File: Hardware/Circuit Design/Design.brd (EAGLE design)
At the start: 94 x 38.1 mm, 41 parts, among them J1 6495, U1 ATMEGA328-PU, U2 TP4056, U3 HTU21D, U4 MT3608, Y1 16 MHz HC-49US

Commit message: Design display for co2 monitor
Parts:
- added U$2: LOGO, PCB Logo:FOOTPRINT
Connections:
- net +5V: now also FTDI_PROG.TX, U$1.VIN; no longer FTDI_PROG.VCC, U$1.PWM
- net GND: now also U$1.GND; no longer U$1.AOT
- net MHZ-TX: now also U$1.RX; no longer U$1.SR
- net RX: now also FTDI_PROG.VCC; no longer FTDI_PROG.TX
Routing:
- net MHZ-TX: track 58.0 -> 62.5 mm

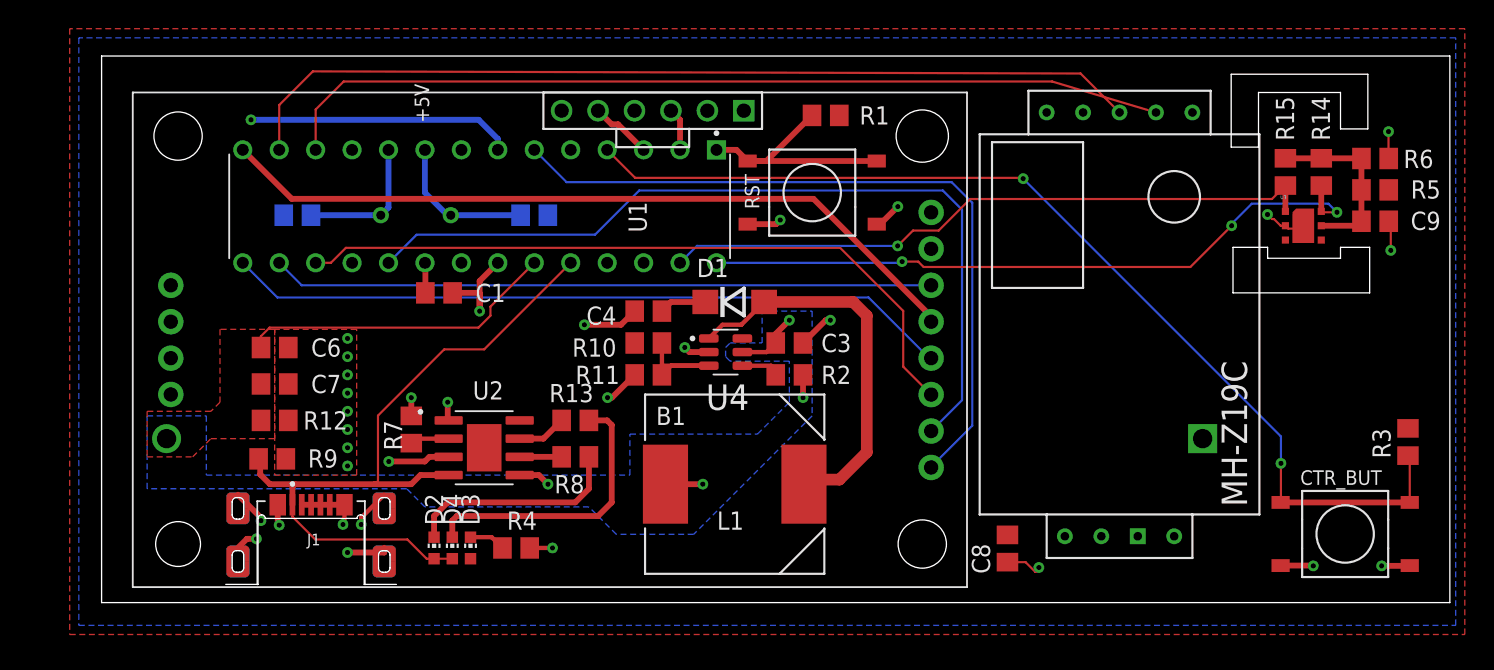
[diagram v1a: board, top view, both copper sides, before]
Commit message: Correct the sleep mode enter function and add the new board design
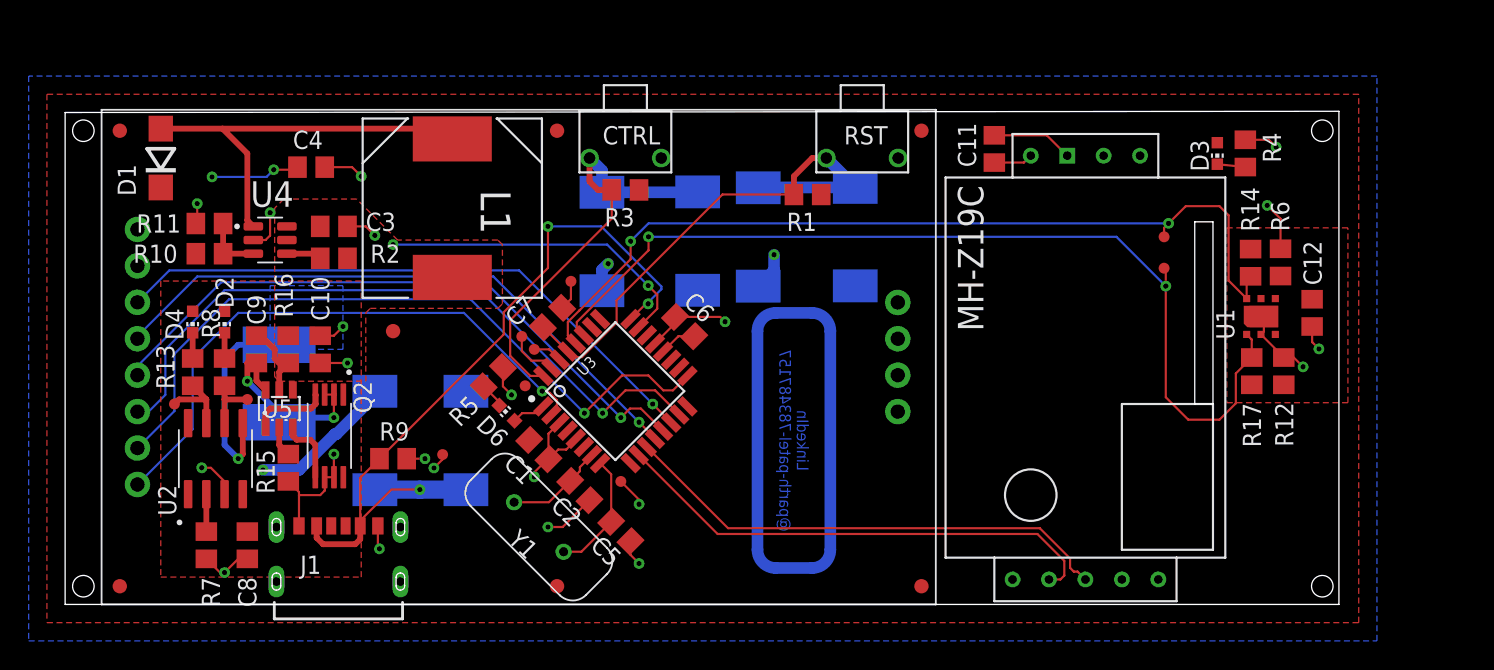
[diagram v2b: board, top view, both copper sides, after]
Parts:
- removed B1: 1S, 18650 1S PCB Mount:18650-1S-DIP
- removed FTDI_PROG: UART, FTDI Adapter:UART
- added BAT+, BAT-: WIREPADSMD5-2,5, wirepad:5-2,5
- added C10: 10u, rcl:C0805
- added C11: 47u, rcl:C0805
- added C12: 100n, rcl:C0805
- added D10, D11, D12, D7, D8, D9: SS310, Schottky SS310:DIOM6859X262N
- added D6: 5215, led:CHIP-LED0603
- added FID1, FID2, FID3, FID4, FID5, FID6, FID7: FIDUCIAL"", Airquality_Sensor:FIDUCIAL_1MM
- added Q2: FS8205A, FS8205A:SOP65P640X120-8N
- added R16: 100R, rcl:R0805
- added R17: 10k, rcl:R0805
- added TP1, TP10, TP2, TP3, TP4, TP5, TP6, TP7: TEST-POINT3, SparkFun-Connectors:PAD.03X.03
- added TP8: ~STDBY, SparkFun-Connectors:PAD.03X.03
- added TP9: ~CHRG, SparkFun-Connectors:PAD.03X.03
- added U5: DW01A, DW01A:SOT23-6
- C6: value 10u -> 100n
- C7: value 100n -> 10u
- C8: value 47u -> 10u
- CTR_BUT, RST: value 4.5X4.5-SMD-TACTILE-SWITCH -> 7058; device Switches:SMD-4.5X4.5-TACTILE-PUSH-BUTTON -> Switches:DIP_3X6MM_SIDE_PRESS_2PIN
- D2: value BLUE -> 5216
- D3: value RED -> 5215
- D4: value ORANGE -> 5215
- J1: value 6495 -> 5362; device MicroUSB Type B Socket:AMPHENOL_10103593-0001LF -> MicroUSB Type C Socket:GCT_USB4125-GF-A-0190_REVA2
- L1: value 220uH -> 22uH
- R12: value 10k -> 3k
- R15: value 10k -> 1k
- R5: value 1.8k -> 220R
- R6: value 3k -> 1.8k
- R7: value 1.2k -> 3k
- U$1: value MH-Z19C -> LOGO_17MM; device MH-Z19 Sensor:MH-Z19C -> PCB Logo:FOOTPRINT_17MM
- U$2: value LOGO -> MH-Z19C; device PCB Logo:FOOTPRINT -> MH-Z19 Sensor:MH-Z19C
- U1: value ATMEGA328-PU -> HTU21D; device ATMEGA328-PU:DIP787W46P254L3467H508Q28 -> HTU21D:QFN100P300X300X100-7N
- U3: value HTU21D -> ATMEGA328P-AU; device HTU21D:QFN100P300X300X100-7N -> ATMEGA328P-AU:QFP80P900X900X120-32N
- Y1: value 16 MHz HC-49US -> HC-49US
- moved C9 78.5 mm to (10.8, 17.8), turned to 270 degrees
- moved R15 72.5 mm to (13.0, 9.53), turned to 270 degrees
- moved R12 70.4 mm to (82.4, 16.3), turned to 270 degrees
- moved DISPLAY 70.1 mm to (0.00, 0.00), turned to 0 degrees
- moved R5 62.8 mm to (27.3, 15.9), turned to 45 degrees
- moved D3 58.9 mm to (77.8, 31.4), turned to 180 degrees
- moved R4 57.8 mm to (79.7, 31.4), turned to 90 degrees
- moved R3 57.3 mm to (36.5, 28.9), turned to 180 degrees
- moved CTR_BUT 56.6 mm to (36.5, 31.1), turned to 180 degrees
- moved U1 55.0 mm to (80.8, 20.1), turned to 90 degrees
- moved C8 53.0 mm to (10.2, 4.13)
- moved U3 49.3 mm to (35.8, 14.9), turned to 45 degrees
- moved D1 41.2 mm to (4.13, 31.1), turned to 90 degrees
- moved C3 32.8 mm to (16.2, 26.4)
- moved R2 32.8 mm to (16.2, 24.1)
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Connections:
- removed net MHZ-RX: U$1.TX, U1.13
- removed net MHZ-TX: U$1.RX, U1.12
- removed net MISO: U1.18
- removed net N$1: R8.2, U2.6
- removed net N$4: R7.2, U2.2
- new net BAT-: BAT-.1, C9.2, Q2.2, Q2.3, U5.6
- new net DTR: C7.2, TP1.P$1
- new net MHZ_N: U$2.RX, U3.10
- new net MHZ_P: U$2.TX, U3.11
- new net N$13: D6.C, R5.1
- new net N$14: D6.A, U3.1
- new net N$15: Q2.5, U5.3
- new net N$16: R13.2, TP9.P$1, U2.7
- new net N$17: R8.2, TP8.P$1, U2.6
- new net N$18: R7.1, U2.2
- new net N$19: Q2.4, U5.1
- new net N$20: R15.1, U5.2
- new net N$21: C9.1, R16.1, U5.5
- new net SUP-IN: D7.A, D8.C, J1.A9, J1.B9, R9.1, U3.24
- net +3V3: now also C12.1, R12.2, R17.2, R6.1, U1.5; no longer C9.1, R15.2, R5.1, R6.2, U3.5
- net +5V: now also C11.1, D11.C, D9.C, DISPLAY.VCC, R6.2, TP4.P$1, U$2.VIN, U3.18, U3.4, U3.6; no longer C8.1, DISPLAY.P$16, FTDI_PROG.TX, R5.2, U$1.VIN, U1.20, U1.7
- net CTR-BTN: now also CTR_BUT.P$1, D10.C, D9.A, U3.32; no longer CTR_BUT.1.1, CTR_BUT.1.2, U1.4
- net GND: now also C10.2, C11.2, C12.2, CTR_BUT.P$2, D10.A, D12.A, D8.A, DISPLAY.GND, J1.A12, J1.B12, Q2.6, Q2.7, R15.2, R5.2, R7.2, RST.P$2, TP5.P$1, TP7.P$1, U$2.GND, U1.2, U1.PAD, U3.21, U3.3, U3.5; no longer B1.V-, C7.2, C9.2, CTR_BUT.2.1, CTR_BUT.2.2, DISPLAY.P$15, FTDI_PROG.GND, J1.2, J1.3, J1.4, J1.5, J1.S1, J1.S2, J1.S3, J1.S4, J1.S5, J1.S6, R6.1, R7.1, RST.2.1, RST.2.2, U$1.GND, U1.22, U1.8, U2.1, U3.2, U3.PAD
- net MOSI: now also DISPLAY.SDA, U3.15; no longer DISPLAY.P$11, U1.17
- net N$10: now also U3.7; no longer U1.9
- net N$2: now also U3.8; no longer U1.10
- net N$6: now also C6.1, U3.20; no longer R13.2, U2.7
- net RST: now also C7.1, D11.A, D12.C, RST.P$1, U3.29; no longer RST.1.1, RST.1.2, U1.1
- net RX: now also TP2.P$1, U3.30; no longer FTDI_PROG.VCC, U1.2
- net SCK: now also DISPLAY.SCK, U3.17; no longer DISPLAY.P$10, U1.19
- net SCL: now also TP6.P$1, U1.6, U3.28; no longer U1.28, U3.6
- net SDA: now also R17.1, TP10.P$1, U1.1, U3.27; no longer R15.1, U1.27, U3.1
- net TFT-CS: now also DISPLAY.CS, U3.14; no longer DISPLAY.P$14, U1.16
- net TFT-DC: now also DISPLAY.DC, U3.13; no longer DISPLAY.P$12, U1.15
- net TFT-LED: now also DISPLAY.LED, U3.2; no longer DISPLAY.P$9, U1.6
- net TFT-RST: now also DISPLAY.RST, U3.12; no longer DISPLAY.P$13, U1.14
- net TX: now also TP3.P$1, U3.31; no longer FTDI_PROG.RX, U1.3
- net VBAT: now also BAT+.1, C10.1, R16.2, U3.23; no longer B1.V+, C6.1, C7.1, R12.2, U1.23
- net VCC: now also C8.1, D7.C, U2.8; no longer J1.1, R9.1, U1.24
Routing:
- net MHZ-RX: track 63.8 -> 0.00 mm
- net MHZ-TX: track 62.5 -> 0.00 mm
- net SUP-IN: track 0.00 -> 57.3 mm, vias 0 -> 3
- net VCC: track 52.2 -> 10.3 mm, vias 0 -> 1
- net CTR-BTN: track 72.2 -> 30.2 mm, vias 2 -> 0
- net MHZ_N: track 0.00 -> 34.9 mm
- net MHZ_P: track 0.00 -> 34.8 mm
- net SDA: track 46.2 -> 67.1 mm, vias 1 -> 2
- net RST: track 17.3 -> 37.7 mm
- net N$8: track 19.9 -> 1.79 mm
- net BAT-: track 0.00 -> 14.0 mm, vias 0 -> 2
- net N$9: track 15.3 -> 1.79 mm
- net SCL: track 48.5 -> 61.2 mm, vias 3 -> 2
- net +3V3: track 12.6 -> 0.00 mm
- net TFT-LED: track 51.7 -> 40.8 mm, vias 0 -> 1
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- added copper zone on layer 1, net +3V3
- added copper zone on layer 1, net VCC
- removed copper zone on layer 1, net GND
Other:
- board size 94 x 38.1 mm -> 88.8 x 34.4 mm
- board text added: "CTRL"
- board text added: "RST"
- board text removed: "+5V"
